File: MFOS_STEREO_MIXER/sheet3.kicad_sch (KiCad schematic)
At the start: 29 parts, among them J14 Jack-DC, J17 AudioJack2_Ground, J7 Jack-DC, U5 TL072, U8 LM386, U9 LM386

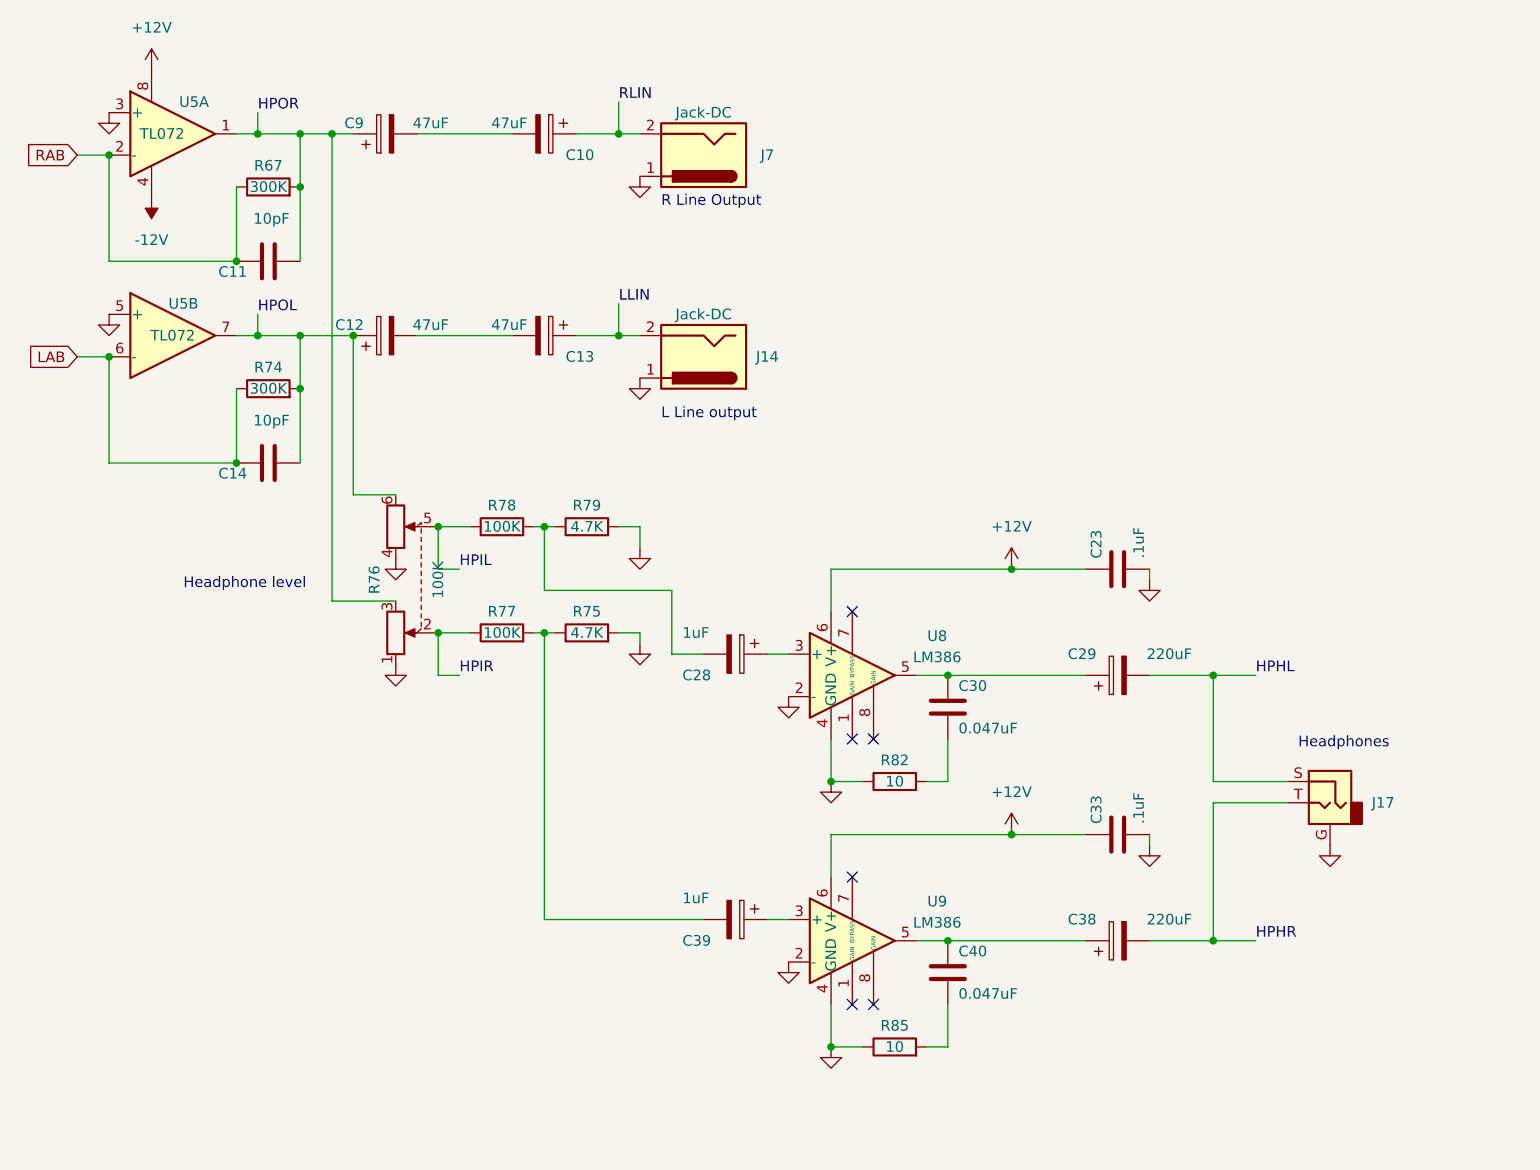
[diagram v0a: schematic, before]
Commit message: Split up design into different sheets
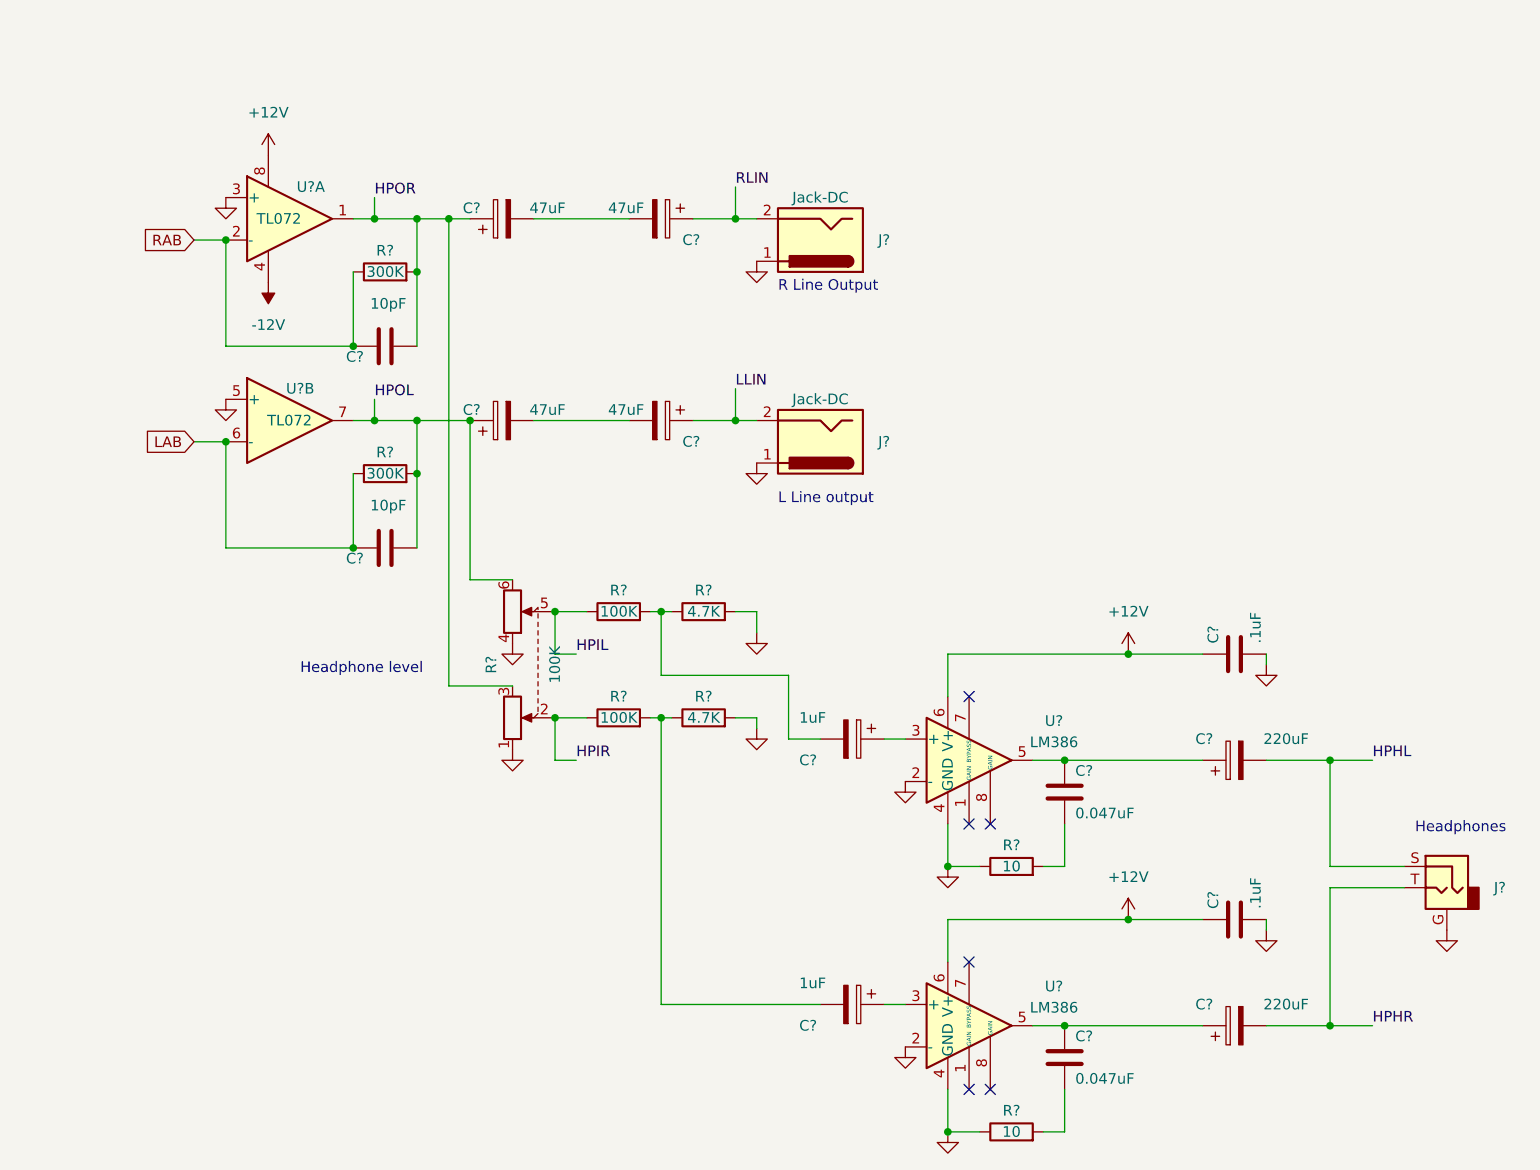
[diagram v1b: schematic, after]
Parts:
- removed C10, C12, C13, C9: 47uF, symbol Device:C_Polarized
- removed C11, C14: 10pF, symbol Device:C
- removed C23, C33: .1uF, symbol Device:C
- removed C28, C39: 1uF, symbol Device:C_Polarized
- removed C29, C38: 220uF, symbol Device:C_Polarized
- removed C30, C40: 0.047uF, symbol Device:C
- removed J14, J7: Jack-DC, symbol Connector:Jack-DC
- removed J17: AudioJack2_Ground, symbol Connector:AudioJack2_Ground
- removed R67, R74: 300K, symbol Device:R
- removed R75, R79: 4.7K, symbol Device:R
- removed R76: 100K, symbol dhk:R_Potentiometer_Dual_Audio_Taper
- removed R77, R78: 100K, symbol Device:R
- removed R82, R85: 10, symbol Device:R
- removed U5: TL072, symbol Amplifier_Operational:TL072
- removed U8, U9: LM386, symbol Amplifier_Audio:LM386
- added C? (x2): 220uF, symbol Device:C_Polarized
- added C? (x2): 1uF, symbol Device:C_Polarized
- added C? (x4): 47uF, symbol Device:C_Polarized
- added C? (x2): 0.047uF, symbol Device:C
- added C? (x2): .1uF, symbol Device:C
- added C? (x2): 10pF, symbol Device:C
- added J? (x2): Jack-DC, symbol Connector:Jack-DC
- added J?: AudioJack2_Ground, symbol Connector:AudioJack2_Ground
- added R? (x2): 100K, symbol Device:R
- added R? (x2): 4.7K, symbol Device:R
- added R? (x2): 300K, symbol Device:R
- added R? (x2): 10, symbol Device:R
- added R?: 100K, symbol dhk:R_Potentiometer_Dual_Audio_Taper
- added U? (x3): TL072, symbol Amplifier_Operational:TL072
- added U? (x2): LM386, symbol Amplifier_Audio:LM386
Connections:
- net +12V: now also C?.1, C?.1, U?.6 (V+), U?.6 (V+), U?.8 (V+)
- net -12V: now also U?.4 (V-)
- net GND: now also C?.2, C?.2, J?.1, J?.1, J?.G, R?.1, R?.1, R?.1, R?.2, R?.2, R?.4, U?.2 (-), U?.2 (-), U?.3 (+), U?.4 (GND), U?.4 (GND), U?.5 (+)
- net HPHL: now also C?.2, J?.S
- net HPHR: now also C?.2, J?.T
- net HPIL: now also R?.1, R?.5
- net HPIR: now also R?.1, R?.2
- net HPOL: now also C?.1, C?.2, R?.2, R?.6, U?.7
- net HPOR: now also C?.1, C?.2, R?.2, R?.3, U?.1
- net LAB: now also C?.1, R?.1, U?.6 (-)
- net LLIN: now also C?.1, J?.2
- net RAB: now also C?.1, R?.1, U?.2 (-)
- net RLIN: now also C?.1, J?.2
- new net: C?.1, C?.1, U?.5 (x2)
- new net: C?.2, R?.1, R?.2 (x2)
- new net: C?.2, R?.2 (x2)
- new net: C?.1, U?.3 (+) (x2)
- new net: C?.2, C?.2 (x2)
